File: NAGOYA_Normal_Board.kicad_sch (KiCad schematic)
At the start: 103 parts, among them CN1 XT30-M, CN13 value, CN14 RefereeSystem, CN15 micro_B, CN2 XT30-M, CN3 XT30-F, CN4 XT30-F, CN5 XT30-F, CN6 XT30-F, J1 debug, J10 CAN3, J13 CAN3, J14 CAN3, J5 CAN3, J6 CAN3, J7 CAN3, J8 CAN3, J9 CAN3, Q2 DDTC114EUA-7-F, Q4 DDTC114EUA-7-F, Q5 DDTC114EUA-7-F, Q6 DDTC114EUA-7-F, SW1 SW_DIP_x04, U1 Teensy4.1, U2 TCAN1042HVDR, U3 TCAN1042HVDR, U4 TCAN1042HVDR, U5 FT234XD, U6 TLP172AM, U7 BNO055, U8 ADuM121N, U9 LXES11DAA2-137, Y2 32.768 k

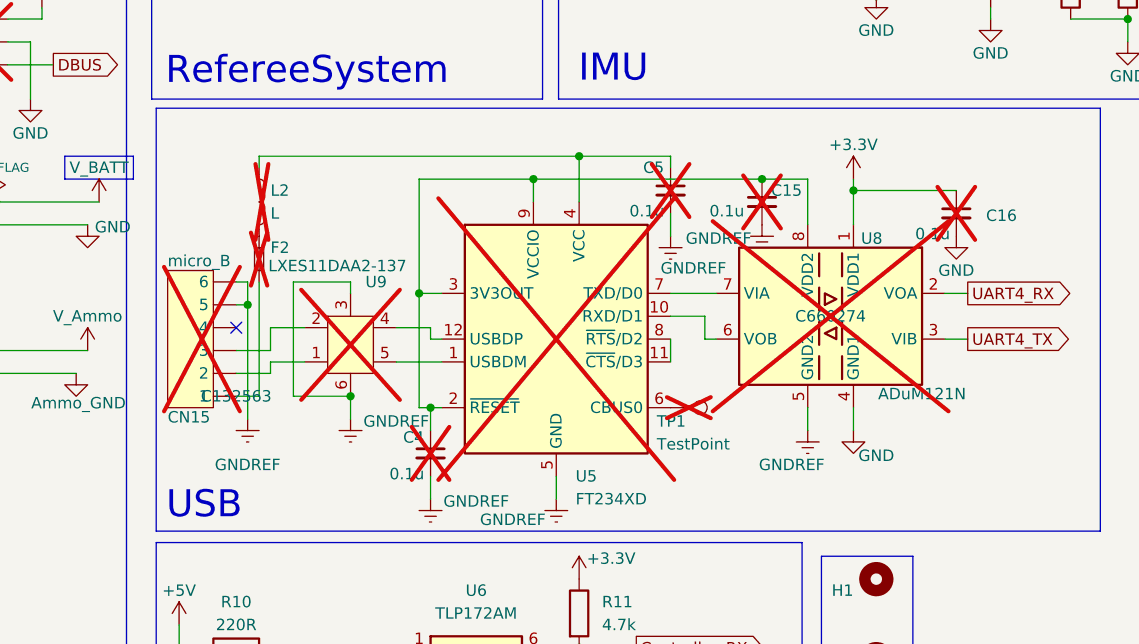
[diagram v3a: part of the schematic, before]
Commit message: 3Dモデルを割当
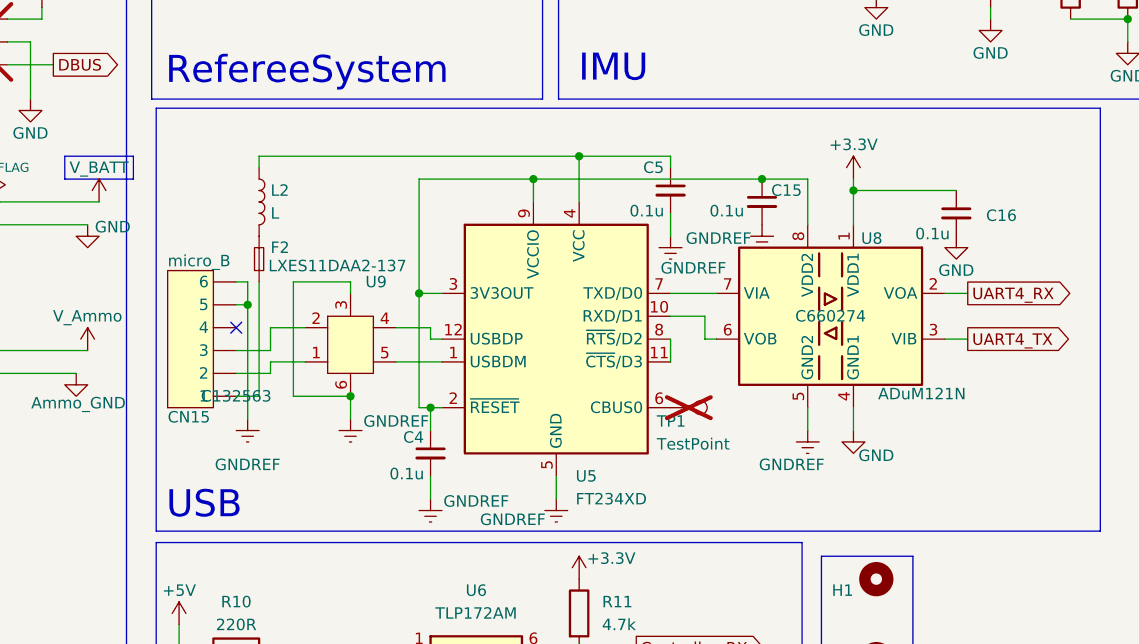
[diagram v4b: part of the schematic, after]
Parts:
- C15, C16, C4, C5, CN15, F2, L2, U5, U8, U9: now fitted
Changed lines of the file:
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@@
 		(in_bom yes)
 		(on_board yes)
-		(dnp yes)
+		(dnp no)
 		(fields_autoplaced yes)
 		(property "Reference" "F2"
@@
 		(in_bom yes)
 		(on_board yes)
-		(dnp yes)
+		(dnp no)
 		(fields_autoplaced yes)
 		(property "Reference" "U5"
@@
 		(in_bom yes)
 		(on_board yes)
-		(dnp yes)
+		(dnp no)
 		(property "Reference" "U9"
 			(at 112.1411 134.62 0)
@@
 		(in_bom yes)
 		(on_board yes)
-		(dnp yes)
+		(dnp no)
 		(property "Reference" "C5"
 			(at 143.002 121.92 0)
@@
 		(in_bom yes)
 		(on_board yes)
-		(dnp yes)
+		(dnp no)
 		(property "Reference" "C16"
 			(at 181.102 127.254 0)
@@
 		(in_bom yes)
 		(on_board yes)
-		(dnp yes)
+		(dnp no)
 		(property "Reference" "C15"
 			(at 157.226 124.46 0)
@@
 		(in_bom yes)
 		(on_board yes)
-		(dnp yes)
+		(dnp no)
 		(property "Reference" "U8"
 			(at 168.402 129.794 0)
@@
 		(in_bom yes)
 		(on_board yes)
-		(dnp yes)
+		(dnp no)
 		(property "Reference" "C4"
 			(at 116.332 151.892 0)
@@
 		(in_bom yes)
 		(on_board yes)
-		(dnp yes)
+		(dnp no)
 		(fields_autoplaced yes)
 		(property "Reference" "L2"
@@
 		(in_bom yes)
 		(on_board yes)
-		(dnp yes)
+		(dnp no)
 		(fields_autoplaced yes)
 		(property "Reference" "CN15"

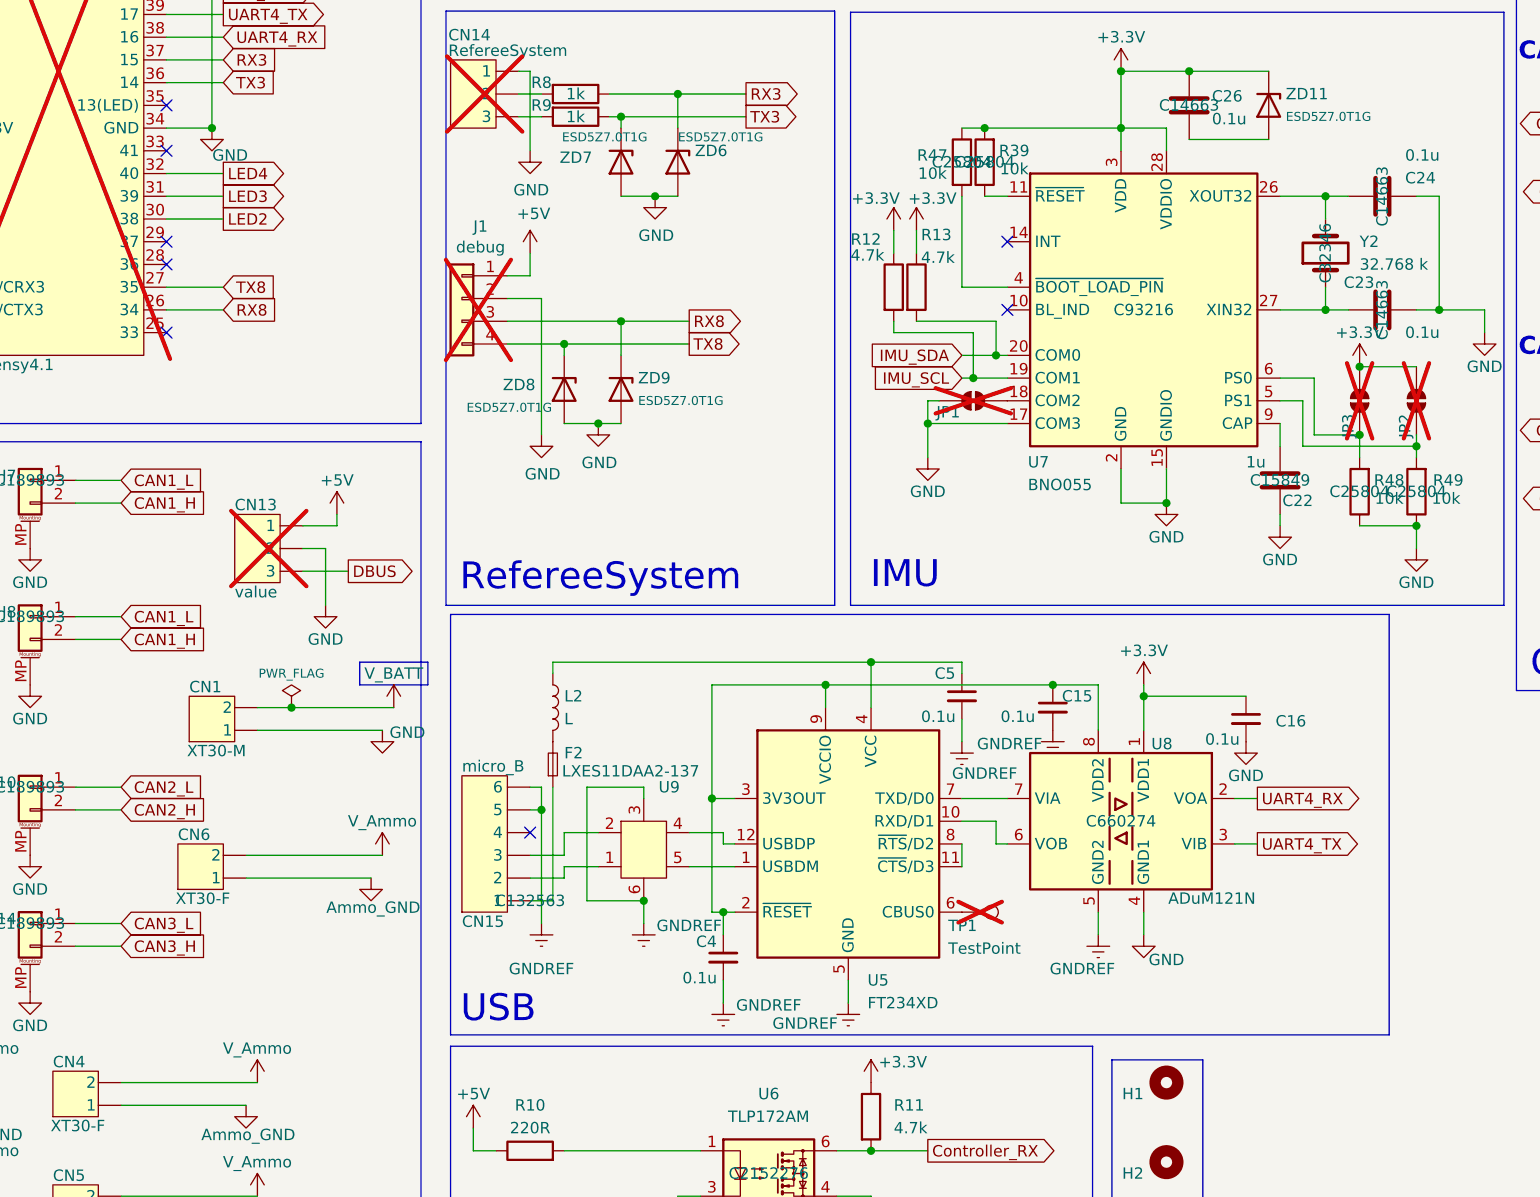
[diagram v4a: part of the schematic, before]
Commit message: USBを削除パターンを変更
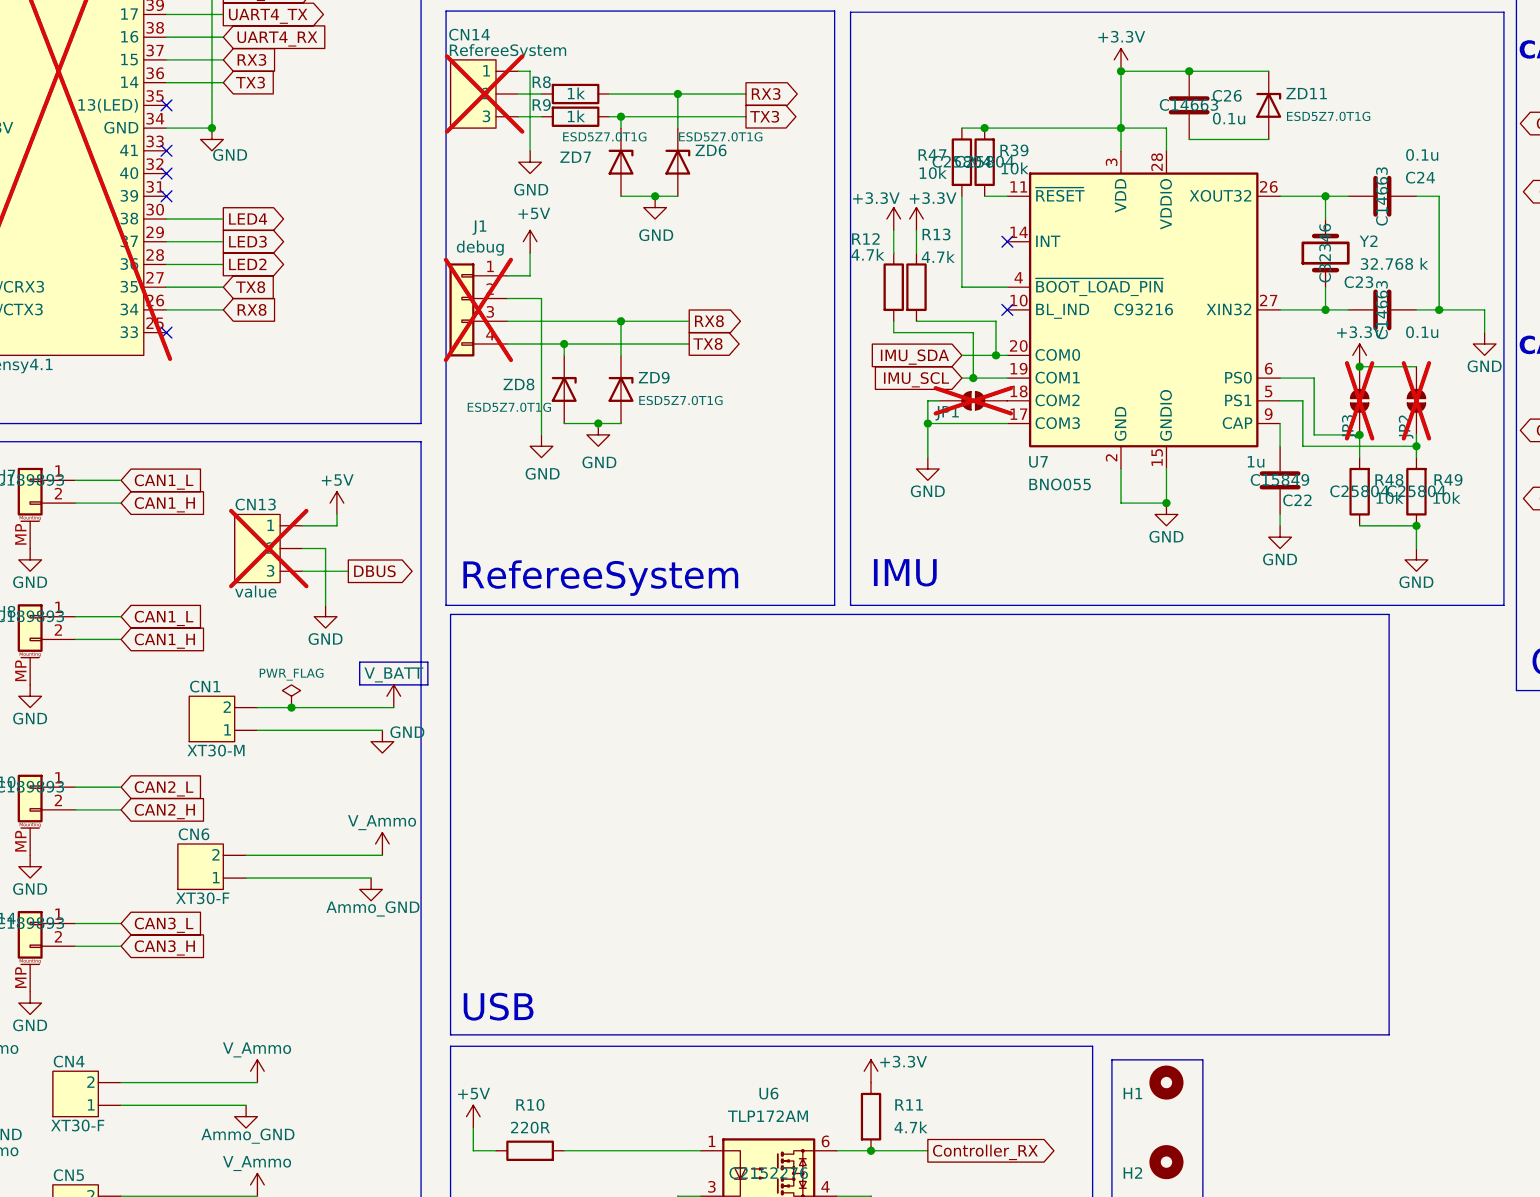
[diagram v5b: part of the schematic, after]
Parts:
- removed C15, C16, C4, C5: 0.1u, Capacitor_SMD:C_0603_1608Metric, symbol Device:C_Small
- removed CN15: micro_B, Connector_USB:USB_Micro-B_Amphenol_10118194-0001LF_Horizontal, symbol 0_circuit:CON_6P
- removed F2: Fuse_Small, Fuse:Fuse_0603_1608Metric, symbol Device:Fuse_Small
- removed L2: L, Inductor_SMD:L_0603_1608Metric, symbol Device:L
- removed TP1: TestPoint, TestPoint:TestPoint_Pad_1.0x1.0mm, symbol Connector:TestPoint
- removed U5: FT234XD, Package_DFN_QFN:WDFN-12-1EP_3x3mm_P0.45mm_EP1.7x2.5mm, symbol Interface_USB:FT234XD
- removed U8: ADuM121N, Package_SO:SOIC-8_3.9x4.9mm_P1.27mm, symbol Isolator:ADuM121N
- removed U9: LXES11DAA2-137, 0_PCB:FIL_LXES11DAA2-137, symbol 0_circuit:LXES11DAA2-137
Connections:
- net LED2: now also U1.28 (36); no longer U1.30 (38)
- net LED3: now also U1.29 (37); no longer U1.31 (39)
- net LED4: now also U1.30 (38); no longer U1.32 (40)
- no-connect marks 17 -> 16
